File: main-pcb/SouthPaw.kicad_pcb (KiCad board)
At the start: 2 copper layers, 98.3 x 131.3 mm, 68 parts, among them SW1 SW_Push, SW10 SW_Push, SW11 SW_Push, SW12 SW_Push, SW13 SW_Push, SW14 SW_Push, SW15 SW_Push, SW16 SW_Push, SW17 SW_Push, SW18 SW_Push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

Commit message: I think Im finished with es2
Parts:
- added H10: MountingHole, PeteCB:m2.5 hole, F.Cu at (23.5, 27.0)
- added H11: MountingHole, PeteCB:m2.5 hole, F.Cu at (59.9, 27.1)
- moved D11 77.0 mm to (30.3, 52.0), turned to 0 degrees
- moved D5 69.9 mm to (103.9, 56.8), turned to 0 degrees
- moved D1 69.4 mm to (33.9, 56.9), turned to 0 degrees
- moved D6 67.1 mm to (32.1, 54.4), turned to 0 degrees
- moved D20 64.6 mm to (106.4, 53.8), turned to 180 degrees
- moved D4 47.2 mm to (81.3, 57.0), turned to 0 degrees
- moved D21 46.8 mm to (26.9, 47.0), turned to 0 degrees
- moved D25 46.1 mm to (109.0, 51.2), turned to 180 degrees
- moved H2 35.1 mm to (60.2, 58.0)
- moved D23 33.8 mm to (39.6, 47.4), turned to 0 degrees
- moved JPSP2 33.2 mm to (53.6, 32.2)
- moved D3 31.5 mm to (69.0, 56.9), turned to 0 degrees
- moved D9 28.1 mm to (79.7, 54.5), turned to 0 degrees
- moved D14 25.4 mm to (77.8, 52.0)
- moved JPSP3 24.6 mm to (72.7, 32.2)
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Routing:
- net GND: track 0.00 -> 646.2 mm, vias 0 -> 5
- net +5V: track 0.00 -> 508.5 mm, vias 0 -> 4
- net /Row1: track 0.00 -> 295.7 mm, vias 0 -> 6
- net /ColA: track 0.00 -> 292.2 mm, vias 0 -> 9
- net /ColE: track 0.00 -> 283.3 mm, vias 0 -> 7
- net /ColD: track 0.00 -> 225.9 mm, vias 0 -> 6
- net Net-(SW5-Pad22): track 0.00 -> 202.2 mm, vias 0 -> 2
- net /Row4: track 0.00 -> 199.8 mm, vias 0 -> 3
- net /ENC2B: track 0.00 -> 193.2 mm, vias 0 -> 7
- net /ENC1B: track 0.00 -> 185.8 mm, vias 0 -> 8
- net /Row5: track 0.00 -> 185.1 mm, vias 0 -> 7
- net Net-(D24-Pad1): track 0.00 -> 180.8 mm, vias 0 -> 8
- net /ENC1A(sharedInSclLedMode): track 0.00 -> 172.2 mm, vias 0 -> 7
- net /Row2: track 0.00 -> 168.9 mm, vias 0 -> 4
- net Net-(JPSP3-Pad1): track 0.00 -> 168.8 mm, vias 0 -> 14
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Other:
- outline, holes or cut-outs redrawn
- board text added: "^ Combined Encoder A Pins"
- board text added: "^ Seprate Encoder Pins"
- board text removed: "Combined -> Encoder A Pins"
- board text removed: "^ Seprate ^ Encoder Pins"

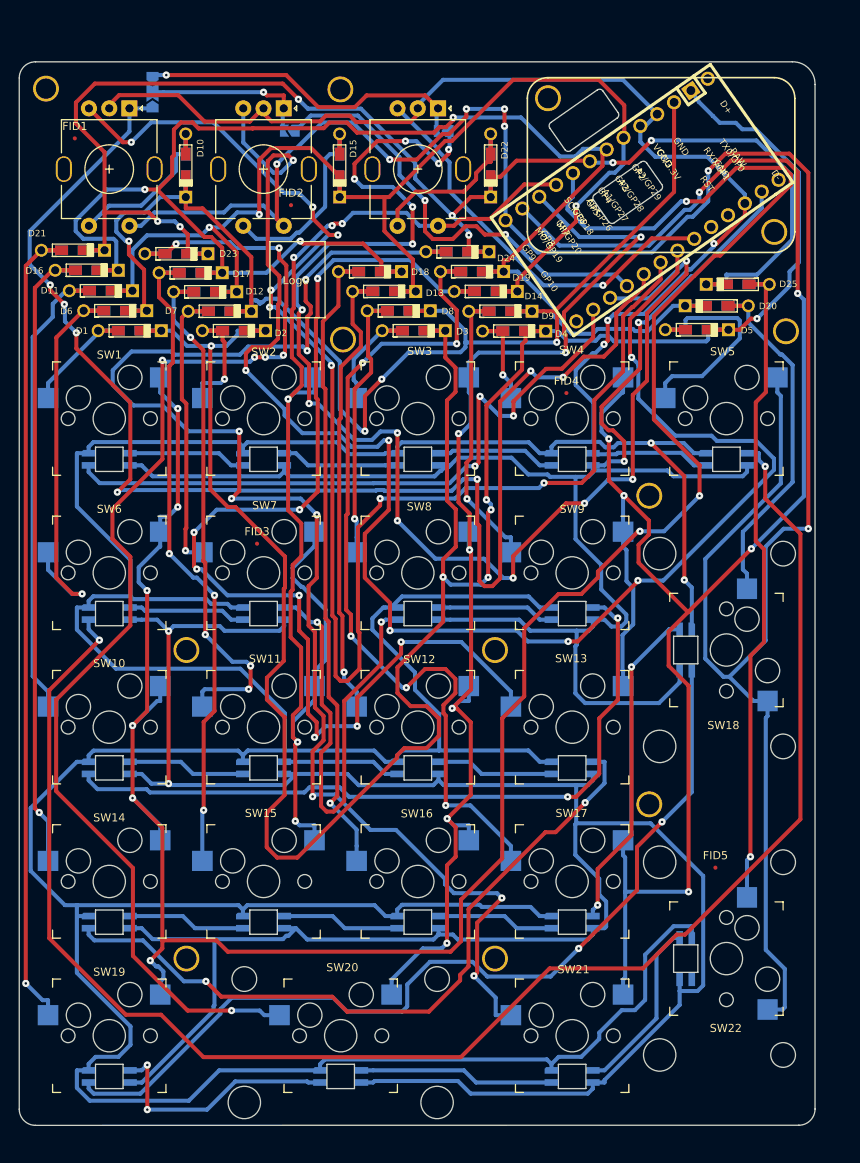
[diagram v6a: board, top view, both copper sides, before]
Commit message: Logo inserted without vias below
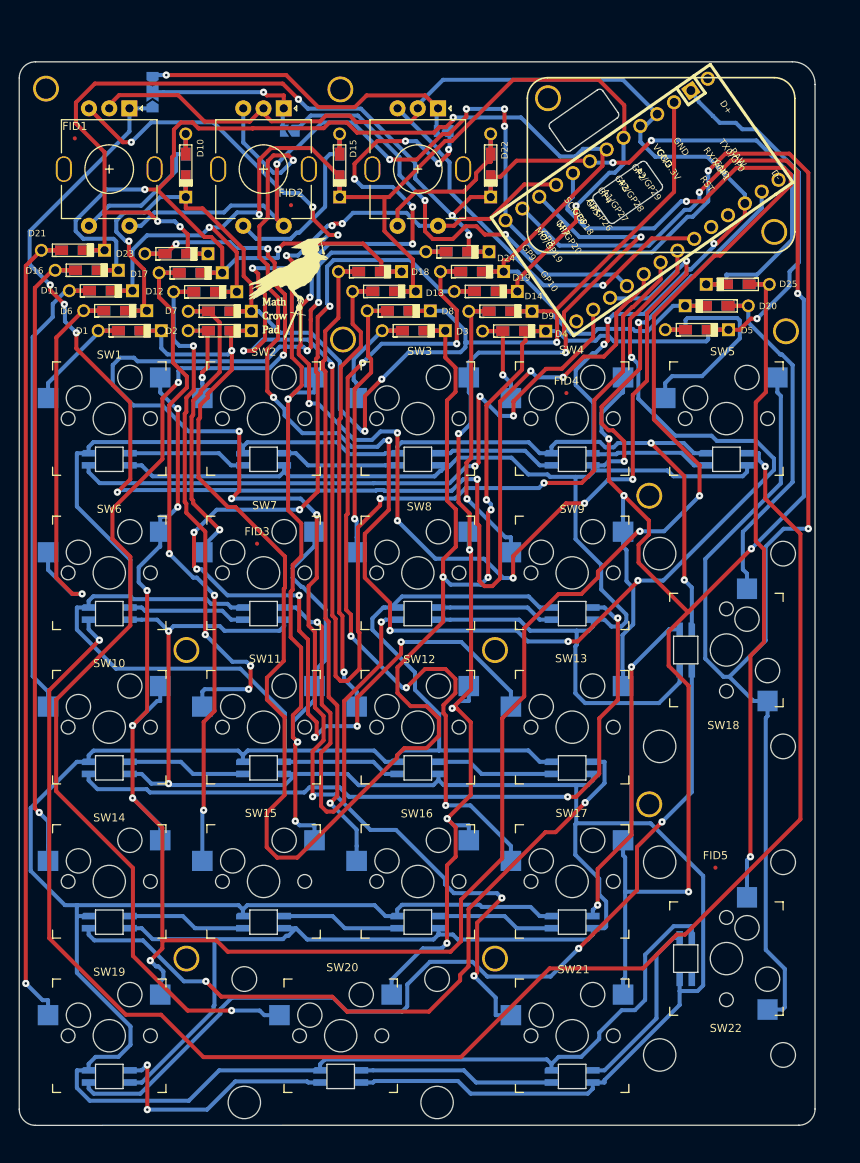
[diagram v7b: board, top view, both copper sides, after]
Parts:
- moved D2 1.76 mm to (45.0, 56.9)
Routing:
- net /ENC1B: track 185.8 -> 199.6 mm
- net Net-(D2-Pad1): track 15.9 -> 8.63 mm
- net Net-(D23-Pad1): track 154.9 -> 151.8 mm, vias 7 -> 5
- net /ENC2B: track 193.2 -> 190.5 mm
- net /Row2: track 168.9 -> 166.4 mm
- net /Row1: track 295.7 -> 293.6 mm
- net Net-(D12-Pad1): track 66.8 -> 68.7 mm
- net Net-(D7-Pad1): track 37.3 -> 39.1 mm
- net Net-(D17-Pad1): track 81.7 -> 83.1 mm
- net /ColB: track 151.7 -> 152.9 mm
- net Net-(JPSP3-Pad1): track 168.8 -> 168.3 mm
